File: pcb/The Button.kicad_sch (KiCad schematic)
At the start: 28 parts, among them J1 Gnd, J2 2169890001, J3 Extra Pins, J4 Buttons, J5 Conn_01x05_Pin, SW8 SW_SPST BOOT, U1 LD1117S33TR_SOT223, U2 STM32C071KBTx, U5 USBLC6-2SC6

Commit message: Update pcb schematic to v3, layout pending
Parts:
- removed C11, C12, C13: 100nF, Capacitor_SMD:C_0805_2012Metric_Pad1.18x1.45mm_HandSolder, symbol Device:C
- removed J1: Gnd, Connector_PinSocket_2.54mm:PinSocket_1x03_P2.54mm_Vertical, symbol Connector:Conn_01x03_Pin
- removed J4: Buttons, Connector_PinSocket_2.54mm:PinSocket_1x04_P2.54mm_Vertical, symbol Connector:Conn_01x04_Pin
- added C1, C2, C5: 100nF, Capacitor_SMD:C_0805_2012Metric_Pad1.18x1.45mm_HandSolder, symbol Device:C
- added H1, H2: MountingHole, MountingHole:MountingHole_3.2mm_M3, symbol Mechanical:MountingHole
- added J1, J4: Conn_01x02, Connector_JST:JST_XH_B2B-XH-AM_1x02_P2.50mm_Vertical, symbol Connector_Generic:Conn_01x02
- added J6: Conn_01x03, Connector_JST:JST_XH_B3B-XH-AM_1x03_P2.50mm_Vertical, symbol Connector_Generic:Conn_01x03
- R1: value 1K -> 5k
- R6, R7: value 5k -> 1k
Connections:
- net BTN_HI: now also C1.1, J1.1 (Pin_1)
- net BTN_KEY: now also C5.1, J6.1 (Pin_1)
- net BTN_LO: now also C2.1, J4.1 (Pin_1)
- net GND: now also C1.2, C2.2, C5.2, J1.2 (Pin_2), J4.2 (Pin_2), J6.2 (Pin_2)
- net VDDA_5V: now also U5.5 (VBUS)
- no-connect marks 18 -> 19
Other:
- company: (none) -> Maebe.me
- title: (none) -> The Button
- moved on the sheet: J3, J5

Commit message: Routing of pcb v3
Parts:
- removed J3: Extra Pins, Connector_PinSocket_2.54mm:PinSocket_1x04_P2.54mm_Vertical, symbol Connector:Conn_01x04_Pin
- added J7: Conn_01x02, Connector_PinHeader_2.54mm:PinHeader_1x02_P2.54mm_Vertical, symbol Connector_Generic:Conn_01x02
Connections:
- net GND: now also J7.2 (Pin_2)
- net at U2.9 (PA2): now also J7.1 (Pin_1)
- no-connect marks 19 -> 21
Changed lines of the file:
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@@
 	)
 	(no_connect
+		(at 213.36 76.2)
+	)
+	(no_connect
 		(at 139.7 181.61)
 	)
@@
 	)
 	(no_connect
+		(at 213.36 73.66)
+	)
+	(no_connect
 		(at 193.04 93.98)
 	)
@@
 	(wire
 		(pts
-			(xy 213.36 73.66) (xy 248.92 73.66)
-		)
-		(stroke
-			(width 0)
-			(type default)
-		)
-	)
-	(wire
-		(pts
 			(xy 20.32 31.75) (xy 20.32 29.21)
 		)
@@
 	(wire
 		(pts
-			(xy 213.36 76.2) (xy 248.92 76.2)
-		)
-		(stroke
-			(width 0)
-			(type default)
-		)
-	)
-	(wire
-		(pts
 			(xy 125.73 143.51) (xy 125.73 146.05)
 		)
@@
 	)
 	(symbol
-		(lib_id "Device:LED")
-		(at 255.27 34.29 90)
+		(lib_id "Connector_Generic:Conn_01x02")
+		(at 254 78.74 0)
 		(unit 1)
 		(exclude_from_sim no)
@@
 		(dnp no)
 		(fields_autoplaced yes)
-		(property "Reference" "D4"
-			(at 259.08 34.6074 90)
+		(property "Reference" "J7"
+			(at 256.54 78.7399 0)
 			(effects
 				(font
 					(size 1.27 1.27)
 				)
-				(justify right)
+				(justify left)
 			)
 		)
-		(property "Value" "USR LED 1"
-			(at 259.08 37.1474 90)
+		(property "Value" "Conn_01x02"
+			(at 256.54 81.2799 0)
 			(effects
 				(font
 					(size 1.27 1.27)
 				)
-				(justify right)
+				(justify left)
 			)
 		)
-		(property "Footprint" "LED_SMD:LED_0805_2012Metric_Pad1.15x1.40mm_HandSolder"
-			(at 255.27 34.29 0)
+		(property "Footprint" "Connector_PinHeader_2.54mm:PinHeader_1x02_P2.54mm_Vertical"
+			(at 254 78.74 0)
 			(effects
 				(font
@@
 		)
 		(property "Datasheet" "~"
-			(at 255.27 34.29 0)
+			(at 254 78.74 0)
 			(effects
 				(font
@@
 			)
 		)
-		(property "Description" "Light emitting diode"
-			(at 255.27 34.29 0)
+		(property "Description" "Generic connector, single row, 01x02, script generated (kicad-library-utils/schlib/autogen/connector/)"
+			(at 254 78.74 0)
 			(effects
 				(font
@@
 			)
 		)
-		(pin "1"
-		)
 		(pin "2"
 		)
+		(pin "1"
+		)
 		(instances
-			(project "The Button"
+			(project ""
 				(path "/6d563493-8b09-4903-a69b-60be5b6cda73"
-					(reference "D4")
+					(reference "J7")
 					(unit 1)
 				)
@@
 	)
 	(symbol
-		(lib_id "power:GND")
-		(at 261.62 54.61 0)
+		(lib_id "Device:LED")
+		(at 255.27 34.29 90)
 		(unit 1)
 		(exclude_from_sim no)
@@
 		(on_board yes)
 		(dnp no)
-		(property "Reference" "#PWR020"
-			(at 261.62 60.96 0)
+		(fields_autoplaced yes)
+		(property "Reference" "D4"
+			(at 259.08 34.6074 90)
 			(effects
 				(font
 					(size 1.27 1.27)
 				)
-				(hide yes)
+				(justify right)
 			)
 		)
-		(property "Value" "GND"
-			(at 265.43 57.15 0)
+		(property "Value" "USR LED 1"
+			(at 259.08 37.1474 90)
 			(effects
 				(font
 					(size 1.27 1.27)
 				)
+				(justify right)
 			)
 		)
-		(property "Footprint" ""
-			(at 261.62 54.61 0)
+		(property "Footprint" "LED_SMD:LED_0805_2012Metric_Pad1.15x1.40mm_HandSolder"
+			(at 255.27 34.29 0)
 			(effects
 				(font
@@
 			)
 		)
-		(property "Datasheet" ""
-			(at 261.62 54.61 0)
+		(property "Datasheet" "~"
+			(at 255.27 34.29 0)
 			(effects
 				(font
@@
 			)
 		)
-		(property "Description" "Power symbol creates a global label with name \"GND\" , ground"
-			(at 261.62 54.61 0)
+		(property "Description" "Light emitting diode"
+			(at 255.27 34.29 0)
 			(effects
 				(font
@@
 		(pin "1"
 		)
+		(pin "2"
+		)
 		(instances
 			(project "The Button"
 				(path "/6d563493-8b09-4903-a69b-60be5b6cda73"
-					(reference "#PWR020")
+					(reference "D4")
 					(unit 1)
 				)
@@
 	(symbol
 		(lib_id "power:GND")
-		(at 203.2 123.19 0)
+		(at 261.62 54.61 0)
 		(unit 1)
 		(exclude_from_sim no)
@@
 		(on_board yes)
 		(dnp no)
-		(property "Reference" "#PWR04"
-			(at 203.2 129.54 0)
+		(property "Reference" "#PWR020"
+			(at 261.62 60.96 0)
 			(effects
 				(font
@@
 		)
 		(property "Value" "GND"
-			(at 207.01 125.73 0)
+			(at 265.43 57.15 0)
 			(effects
 				(font
@@
 		)
 		(property "Footprint" ""
-			(at 203.2 123.19 0)
+			(at 261.62 54.61 0)
 			(effects
 				(font
@@
 		)
 		(property "Datasheet" ""
-			(at 203.2 123.19 0)
+			(at 261.62 54.61 0)
 			(effects
 				(font
@@
 		)
 		(property "Description" "Power symbol creates a global label with name \"GND\" , ground"
-			(at 203.2 123.19 0)
+			(at 261.62 54.61 0)
 			(effects
 				(font
@@
 			(project "The Button"
 				(path "/6d563493-8b09-4903-a69b-60be5b6cda73"
-					(reference "#PWR04")
+					(reference "#PWR020")
 					(unit 1)
 				)
@@
 	)
 	(symbol
-		(lib_id "Connector:Conn_01x04_Pin")
-		(at 254 78.74 180)
+		(lib_id "power:GND")
+		(at 203.2 123.19 0)
 		(unit 1)
 		(exclude_from_sim no)
@@
 		(on_board yes)
 		(dnp no)
-		(property "Reference" "J3"
-			(at 255.27 76.1999 0)
+		(property "Reference" "#PWR04"
+			(at 203.2 129.54 0)
 			(effects
 				(font
 					(size 1.27 1.27)
 				)
-				(justify right)
+				(hide yes)
 			)
 		)
-		(property "Value" "Extra Pins"
-			(at 255.27 78.7399 0)
+		(property "Value" "GND"
+			(at 207.01 125.73 0)
 			(effects
 				(font
 					(size 1.27 1.27)
 				)
-				(justify right)
 			)
 		)
-		(property "Footprint" "Connector_PinSocket_2.54mm:PinSocket_1x04_P2.54mm_Vertical"
-			(at 254 78.74 0)
+		(property "Footprint" ""
+			(at 203.2 123.19 0)
 			(effects
 				(font
@@
 			)
 		)
-		(property "Datasheet" "~"
-			(at 254 78.74 0)
+		(property "Datasheet" ""
+			(at 203.2 123.19 0)
 			(effects
 				(font
@@
 			)
 		)
-		(property "Description" "Generic connector, single row, 01x04, script generated"
-			(at 254 78.74 0)
+		(property "Description" "Power symbol creates a global label with name \"GND\" , ground"
+			(at 203.2 123.19 0)
 			(effects
 				(font
@@
 			)
 		)
-		(pin "3"
-		)
-		(pin "4"
-		)
-		(pin "2"
-		)
 		(pin "1"
 		)
 		(instances
-			(project ""
+			(project "The Button"
 				(path "/6d563493-8b09-4903-a69b-60be5b6cda73"
-					(reference "J3")
+					(reference "#PWR04")
 					(unit 1)
 				)

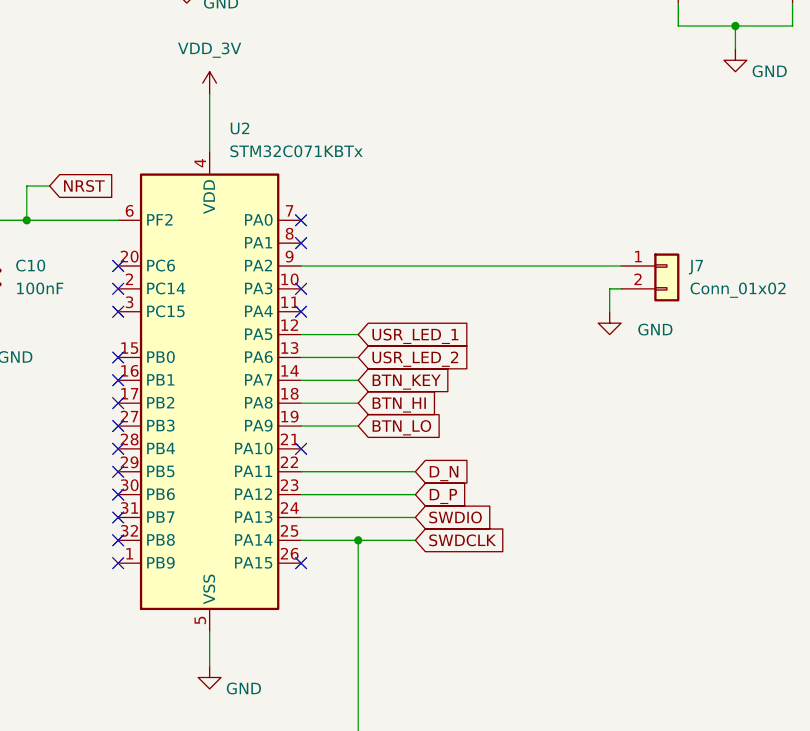
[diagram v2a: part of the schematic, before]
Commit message: Added solder jumpers for hw config
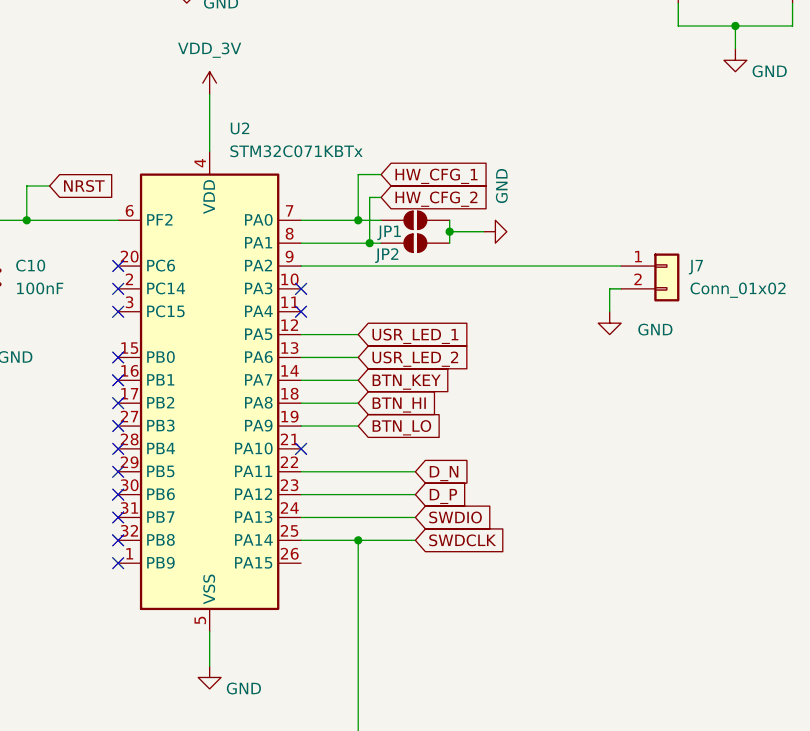
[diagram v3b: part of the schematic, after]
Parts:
- added JP1, JP2: SolderJumper_2_Open, Jumper:SolderJumper-2_P1.3mm_Open_TrianglePad1.0x1.5mm, symbol Jumper:SolderJumper_2_Open
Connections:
- net GND: now also JP1.1 (A), JP2.1 (A)
- net HW_CFG_1: now reaches U2.7 (PA0)
- net HW_CFG_1: now also JP1.2 (B)
- net HW_CFG_2: now reaches U2.8 (PA1)
- net HW_CFG_2: now also JP2.2 (B)
- no-connect marks 21 -> 18
